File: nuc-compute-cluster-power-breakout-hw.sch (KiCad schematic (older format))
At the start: 0 parts

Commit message: Small improvements. Power cycling module sheet
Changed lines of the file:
@@
 $Descr A4 11693 8268
 encoding utf-8
-Sheet 1 2
+Sheet 1 3
 Title "NUC Computer Cluster Power Breakout HW"
 Date "2022-03-03"
@@
 $EndDescr
 $Sheet
-S 7250 3950 3000 1050
+S 7400 2200 3000 1050
 U 62220F27
 F0 "FTDI" 50
 F1 "ftdi-module.sch" 50
 $EndSheet
+$Sheet
+S 7400 3700 3000 950
+U 622E8AAF
+F0 "Power Cycling & Current Measurement" 50
+F1 "pow-cycl-curr-meas.sch" 50
+$EndSheet
 $EndSCHEMATC

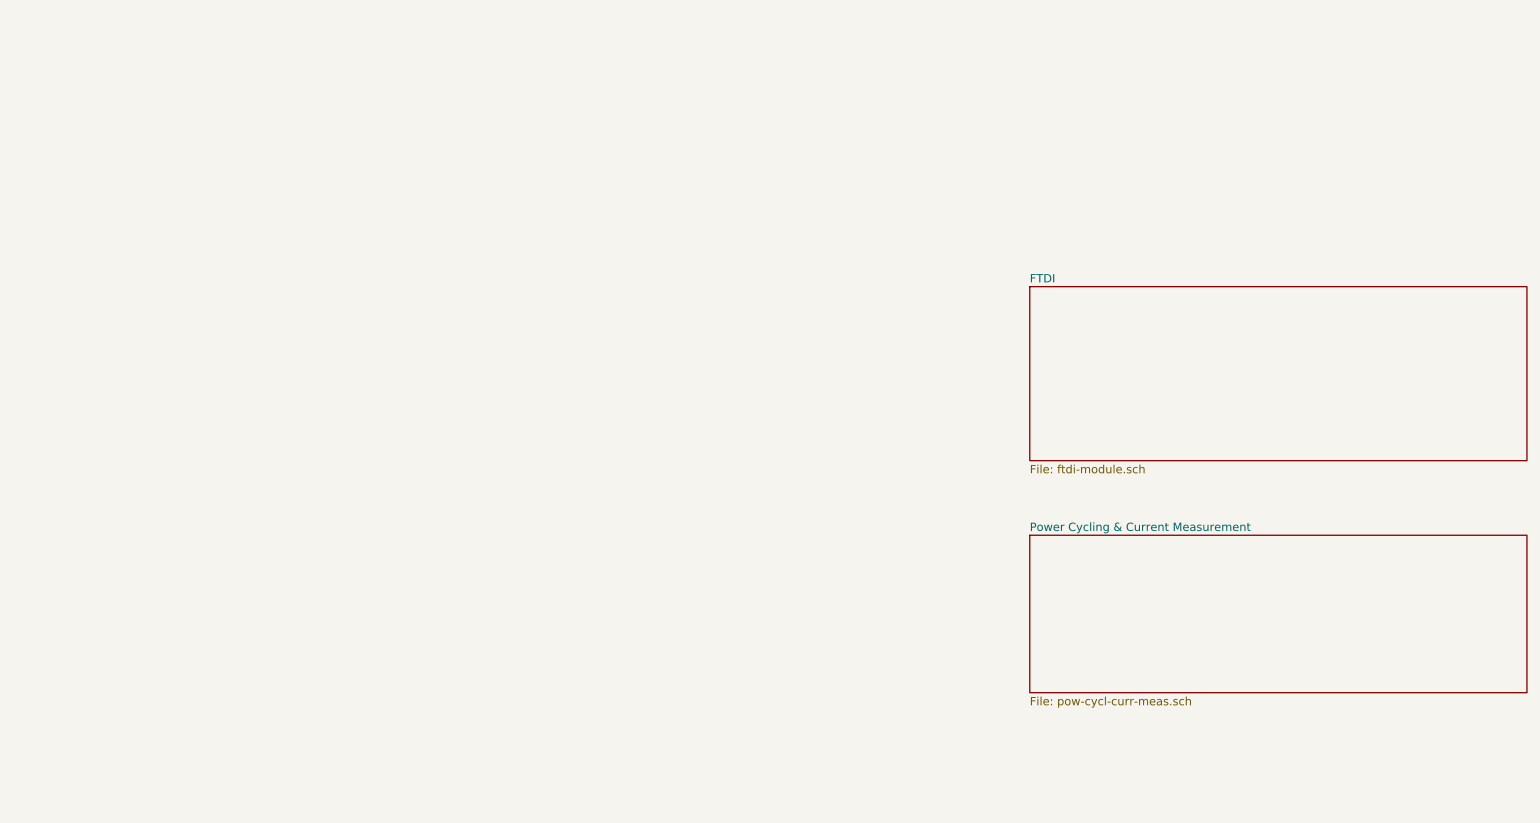
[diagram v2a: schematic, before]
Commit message: Added connection between breakout boards
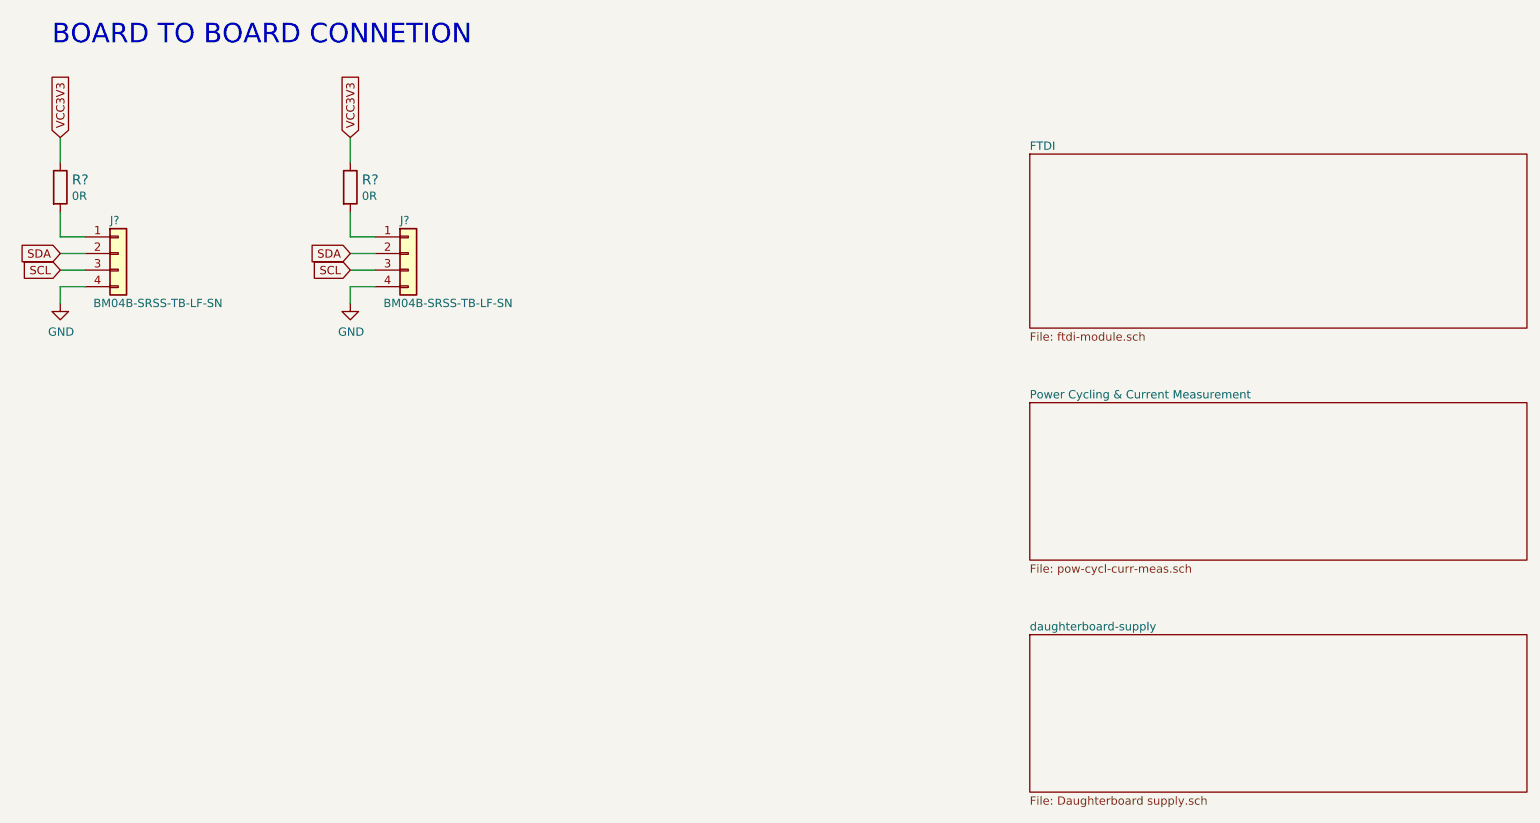
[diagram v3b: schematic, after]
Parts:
- added J? (x2): BM04B-SRSS-TB-LF-SN, antmicro-footprints:BM04B-SRSS-TB-LF-SN, symbol antmicroRectangularConnectorsHeadersMalePins:BM04B-SRSS-TB-LF-SN
- added R? (x2): R_0R_0402, antmicro-footprints:0402-res, symbol antmicroResistors0402:R_0R_0402
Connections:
- new net: J?.1 (Pin_1), R?.2 (x2)
- new net GND: J?.4 (Pin_4), J?.4 (Pin_4)
- new net SCL: J?.3 (Pin_3), J?.3 (Pin_3)
- new net SDA: J?.2 (Pin_2), J?.2 (Pin_2)
- new net VCC3V3: R?.1, R?.1
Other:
- note added: "BOARD TO BOARD CONNETION"
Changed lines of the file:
@@
 $Descr A4 11693 8268
 encoding utf-8
-Sheet 1 3
+Sheet 1 4
 Title "NUC Computer Cluster Power Breakout HW"
 Date "2022-03-03"
@@
 $EndDescr
 $Sheet
-S 7400 2200 3000 1050
+S 7400 1400 3000 1050
 U 62220F27
 F0 "FTDI" 50
@@
 $EndSheet
 $Sheet
-S 7400 3700 3000 950
+S 7400 2900 3000 950
 U 622E8AAF
 F0 "Power Cycling & Current Measurement" 50
 F1 "pow-cycl-curr-meas.sch" 50
 $EndSheet
+$Comp
+L antmicroRectangularConnectorsHeadersMalePins:BM04B-SRSS-TB-LF-SN J?
+U 1 1 6231F410
+P 1900 2150
+F 0 "J?" H 1850 2500 50  0000 L CNN
+F 1 "BM04B-SRSS-TB-LF-SN" H 1750 2000 50  0000 L CNN
+F 2 "antmicro-footprints:BM04B-SRSS-TB-LF-SN" H 1900 1900 50  0001 C CNN
+F 3 "https://www.jst-mfg.com/product/pdf/eng/eSH.pdf" H 1450 1850 50  0001 C CNN
+F 4 "BM04B-SRSS-TB(LF)(SN) " H 1800 1800 50  0001 L CNN "MPN"
+F 5 "JST" H 1800 1700 50  0001 L CNN "Manufacturer"
+	1    1900 2150
+	1    0    0    -1
+$EndComp
+$Comp
+L antmicroRectangularConnectorsHeadersMalePins:BM04B-SRSS-TB-LF-SN J?
+U 1 1 6231FA57
+P 3650 2150
+F 0 "J?" H 3600 2500 50  0000 L CNN
+F 1 "BM04B-SRSS-TB-LF-SN" H 3500 2000 50  0000 L CNN
+F 2 "antmicro-footprints:BM04B-SRSS-TB-LF-SN" H 3650 1900 50  0001 C CNN
+F 3 "https://www.jst-mfg.com/product/pdf/eng/eSH.pdf" H 3200 1850 50  0001 C CNN
+F 4 "BM04B-SRSS-TB(LF)(SN) " H 3550 1800 50  0001 L CNN "MPN"
+F 5 "JST" H 3550 1700 50  0001 L CNN "Manufacturer"
+	1    3650 2150
+	1    0    0    -1
+$EndComp
+$Comp
+L power:GND #PWR?
+U 1 1 6232221D
+P 1550 2300
+F 0 "#PWR?" H 1550 2050 50  0001 C CNN
+F 1 "GND" H 1555 2127 50  0000 C CNN
+F 2 "" H 1550 2300 50  0001 C CNN
+F 3 "" H 1550 2300 50  0001 C CNN
+	1    1550 2300
+	1    0    0    -1
+$EndComp
+Wire Wire Line
+	1550 2300 1550 2200
+Wire Wire Line
+	1550 2200 1700 2200
+$Comp
+L power:GND #PWR?
+U 1 1 62322D69
+P 3300 2300
+F 0 "#PWR?" H 3300 2050 50  0001 C CNN
+F 1 "GND" H 3305 2127 50  0000 C CNN
+F 2 "" H 3300 2300 50  0001 C CNN
+F 3 "" H 3300 2300 50  0001 C CNN
+	1    3300 2300
+	1    0    0    -1
+$EndComp
+Text GLabel 1550 1300 1    50   Input ~ 0
+VCC3V3
+Wire Wire Line
+	3450 2200 3300 2200
+Text GLabel 1550 2100 0    50   Input ~ 0
+SCL
+Text GLabel 1550 2000 0    50   Input ~ 0
+SDA
+Text GLabel 3300 2000 0    50   Input ~ 0
+SDA
+Text GLabel 3300 2100 0    50   Input ~ 0
+SCL
+Wire Wire Line
+	1550 2100 1700 2100
+Wire Wire Line
+	1550 2000 1700 2000
+Text GLabel 3300 1300 1    50   Input ~ 0
+VCC3V3
+$Comp
+L antmicroResistors0402:R_0R_0402 R?
+U 1 1 62328EB6
+P 1550 1600
+F 0 "R?" V 1505 1670 60  0000 L CNN
+F 1 "R_0R_0402" H 1550 1450 60  0001 C CNN
+F 2 "antmicro-footprints:0402-res" H 1750 1800 60  0001 L CNN
+F 3 "" H 1550 1600 50  0001 C CNN
+F 4 "PANASONIC" H 1750 2000 60  0001 L CNN "Manufacturer"
+F 5 "ERJ2GE0R00X" H 1750 1900 60  0001 L CNN "MPN"
+F 6 "0R" V 1603 1670 50  0000 L CNN "Val"
+	1    1550 1600
+	0    1    1    0
+$EndComp
+$Comp
+L antmicroResistors0402:R_0R_0402 R?
+U 1 1 62329827
+P 3300 1600
+F 0 "R?" V 3255 1670 60  0000 L CNN
+F 1 "R_0R_0402" H 3300 1450 60  0001 C CNN
+F 2 "antmicro-footprints:0402-res" H 3500 1800 60  0001 L CNN
+F 3 "" H 3300 1600 50  0001 C CNN
+F 4 "PANASONIC" H 3500 2000 60  0001 L CNN "Manufacturer"
+F 5 "ERJ2GE0R00X" H 3500 1900 60  0001 L CNN "MPN"
+F 6 "0R" V 3353 1670 50  0000 L CNN "Val"
+	1    3300 1600
+	0    1    1    0
+$EndComp
+Wire Wire Line
+	1550 1450 1550 1300
+Wire Wire Line
+	1550 1750 1550 1900
+Wire Wire Line
+	1550 1900 1700 1900
+Wire Wire Line
+	3300 1750 3300 1900
+Wire Wire Line
+	3300 1900 3450 1900
+Wire Wire Line
+	3300 1450 3300 1300
+Wire Wire Line
+	3300 2300 3300 2200
+Wire Wire Line
+	3450 2100 3300 2100
+Wire Wire Line
+	3300 2000 3450 2000
+Text Notes 1500 750  0    118  ~ 0
+BOARD TO BOARD CONNETION
+$Sheet
+S 7400 4300 3000 950
+U 623923F9
+F0 "daughterboard-supply" 50
+F1 "Daughterboard supply.sch" 50
+$EndSheet
 $EndSCHEMATC
